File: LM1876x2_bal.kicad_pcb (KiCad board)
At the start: 2 copper layers, 75 x 45 mm, 38 parts, among them J1 INPUT, J10 STBY, J11 V+, J2 OUTPUT, J3 POWER, J4 Conn_01x01_Male, J5 Conn_01x01_Male, J6 Conn_01x01_Male, J7 Conn_01x01_Male, J8 Conn_01x01_Male, J9 MUTE, U1 LM1876

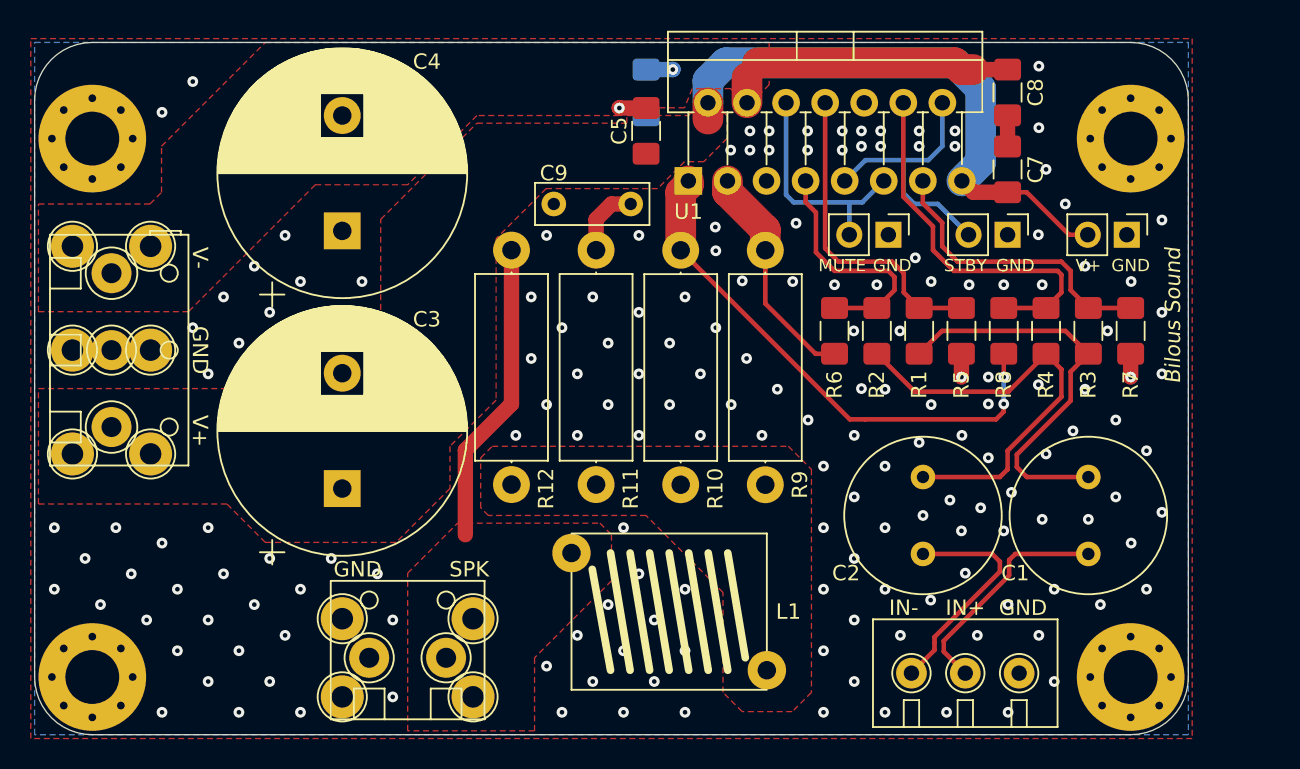
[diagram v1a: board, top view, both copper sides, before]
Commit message: rev2.0 updates include adding mute delay circuit to the board
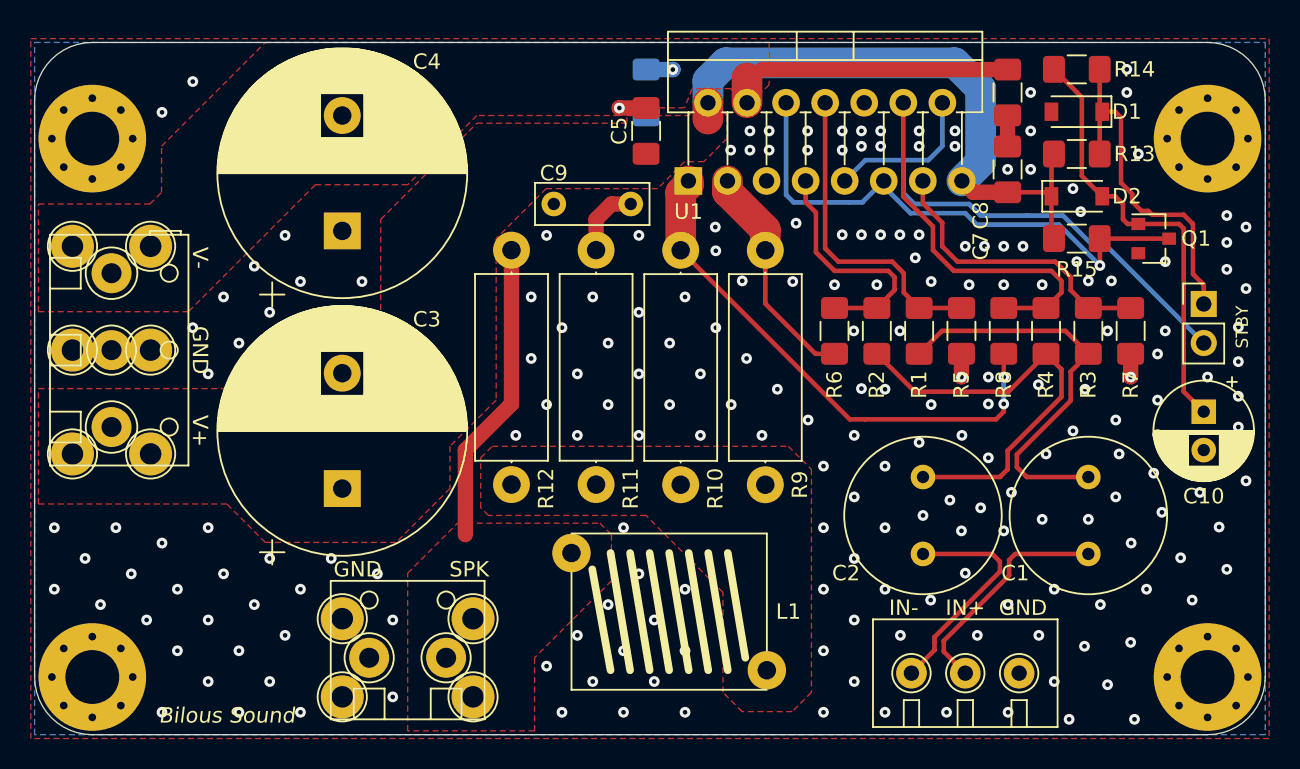
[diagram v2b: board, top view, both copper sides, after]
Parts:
- removed J10: STBY, Connector_PinHeader_2.54mm:PinHeader_1x02_P2.54mm_Vertical
- removed J11: V+, Connector_PinHeader_2.54mm:PinHeader_1x02_P2.54mm_Vertical
- added C10: 22uF, Capacitor_THT:CP_Radial_D6.3mm_P2.50mm, F.Cu at (153.5, 79.0)
- added D1: BZT52Bxx, Diode_SMD:D_SOD-123, F.Cu at (145.2, 59.5)
- added D2: 1N4148W, Diode_SMD:D_SOD-123, F.Cu at (145.2, 65.0)
- added Q1: 2N7002, Package_TO_SOT_SMD:SOT-23, F.Cu at (150.2, 67.8)
- added R13: 10K, Resistor_SMD:R_1206_3216Metric_Pad1.42x1.75mm_HandSolder, F.Cu at (145.2, 62.2)
- added R14: 100K, Resistor_SMD:R_1206_3216Metric_Pad1.42x1.75mm_HandSolder, F.Cu at (145.2, 56.8)
- added R15: 10K, Resistor_SMD:R_1206_3216Metric_Pad1.42x1.75mm_HandSolder, F.Cu at (145.2, 67.8)
- J4: value Conn_01x01_Male -> SPK
- J5, J7: value Conn_01x01_Male -> GND
- J6: value Conn_01x01_Male -> VEE
- J8: value Conn_01x01_Male -> VCC
- J9: value MUTE -> STBY
- moved J9 21.0 mm to (153.5, 72.0), turned to 0 degrees
- moved H3 5.00 mm to (153.8, 61.2)
- moved H4 5.00 mm to (153.8, 96.2)
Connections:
- J9 pad 1: GND -> /5V_ZENER
- J9 pad 2: MUTE -> STBY
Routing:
- net /GATE: track 0.00 -> 29.0 mm
- net /5V_ZENER: track 0.00 -> 22.8 mm
- net MUTE: track 15.2 -> 35.9 mm, vias 0 -> 1
- net STBY: track 17.6 -> 35.8 mm
- net VCC: track 37.5 -> 39.8 mm
- net GND: vias 177 -> 215
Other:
- board size 75 x 45 mm -> 80 x 45 mm
- board text removed: "MUTE"

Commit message: minor changes
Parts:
- moved C10 3.00 mm to (153.5, 76.0)
- moved J9 1.27 mm to (154.8, 71.8), turned to 270 degrees
- moved C7 0.50 mm to (140.8, 63.8)
- moved Q1 0.50 mm to (149.8, 67.8)
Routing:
- net VCC: track 39.8 -> 13.1 mm
- net MUTE: track 35.9 -> 32.9 mm
- net /GATE: track 29.0 -> 26.0 mm
- net /5V_ZENER: track 22.8 -> 20.2 mm
- net STBY: track 35.8 -> 33.4 mm, vias 0 -> 1
- net GND: track 6.81 -> 7.31 mm, vias 215 -> 220
- added copper zone on B.Cu, net VCC
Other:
- board text added: "5V"
- board text added: "Rev2.0"
- board text removed: "Rev1.0"

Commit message: minor fixes
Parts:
- moved C10 1.77 mm to (152.2, 77.2), turned to 0 degrees
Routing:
- net /GATE: track 26.0 -> 27.7 mm
- net GND: vias 220 -> 219
